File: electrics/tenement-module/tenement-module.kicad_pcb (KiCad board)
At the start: 2 copper layers, 86 x 31 mm, 27 parts, among them J2 South, J3 West, J4 East, U1 BA033CC0FP-E2, U2 MCP23009-E_SS, U3 WIRL-WMB8, U4 MAX3486

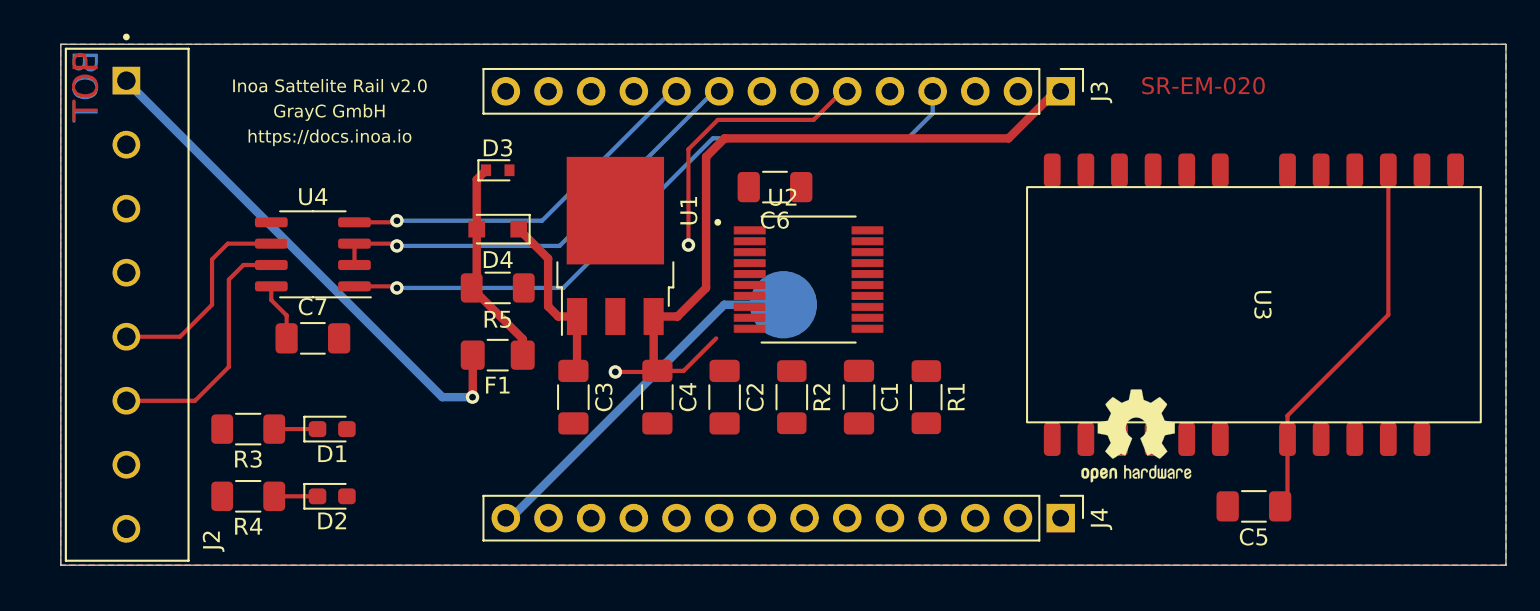
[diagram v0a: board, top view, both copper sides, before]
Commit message: Added product numbers for cost calculation
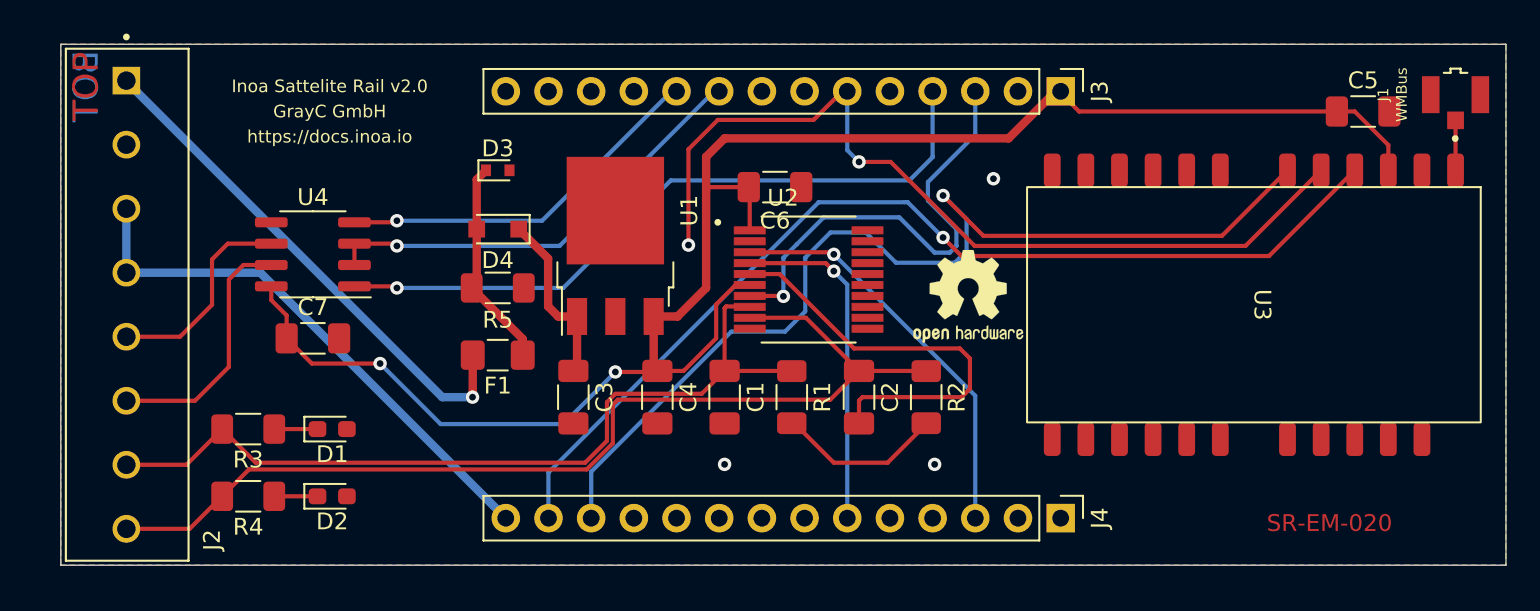
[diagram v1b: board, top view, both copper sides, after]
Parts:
- removed TP1: Shield, TestPoint:TestPoint_Pad_D4.0mm
- added J1: WMBus, footprints:IPEX_20279-001E-01, F.Cu at (183.0, 83.0)
- moved C5 24.4 mm to (177.5, 84.0), turned to 0 degrees
- moved G1 13.0 mm to (154.0, 95.0)
- moved C1 8.00 mm to (139.5, 101.0)
- moved C2 8.00 mm to (147.5, 101.0)
- moved R1 8.00 mm to (143.5, 101.0)
- moved R2 8.00 mm to (151.5, 101.0)
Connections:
- J2 pad 7: RS485_1_A -> S0_0
- J2 pad 8: RS485_1_B -> S0_1
- J3 pad 6: RS485_1_RX -> WMBus_URXD
- J4 pad 12: RS485_1_TXE -> WMBus_~{RTS}
- J4 pad 13: RS485_1_TX -> WMBus_UTXD
- U3 pad 19: +3V3 -> WMBus_~{Reset}
- U3 pad 6: WMBus_RTS -> WMBus_~{RTS}
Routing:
- net WMBus_~{RTS}: track 0.00 -> 60.9 mm, vias 0 -> 1
- net WMBus_UTXD: track 0.00 -> 60.8 mm, vias 0 -> 1
- net S0_1: track 0.02 -> 60.7 mm
- net WMBus_URXD: track 0.00 -> 52.6 mm, vias 0 -> 2
- net S0_0: track 0.02 -> 50.2 mm
- net +3V3: track 70.9 -> 113.6 mm, vias 1 -> 2
- net S0_INT: track 0.00 -> 27.7 mm, vias 0 -> 1
- net GND: track 0.00 -> 25.2 mm, vias 0 -> 3
- net I2C_SCL: track 0.00 -> 24.2 mm, vias 0 -> 1
- net I2C_SDA: track 0.00 -> 20.2 mm, vias 0 -> 1
- net RS485_1_RX: track 16.7 -> 0.00 mm, vias 1 -> 0
- net GNDPWR: track 21.9 -> 32.4 mm
- net WMBus_ANT: track 0.00 -> 2.97 mm
- net RS485_0_RX: track 40.4 -> 41.9 mm

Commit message: INOA-372 Fix out of stock components in TM module
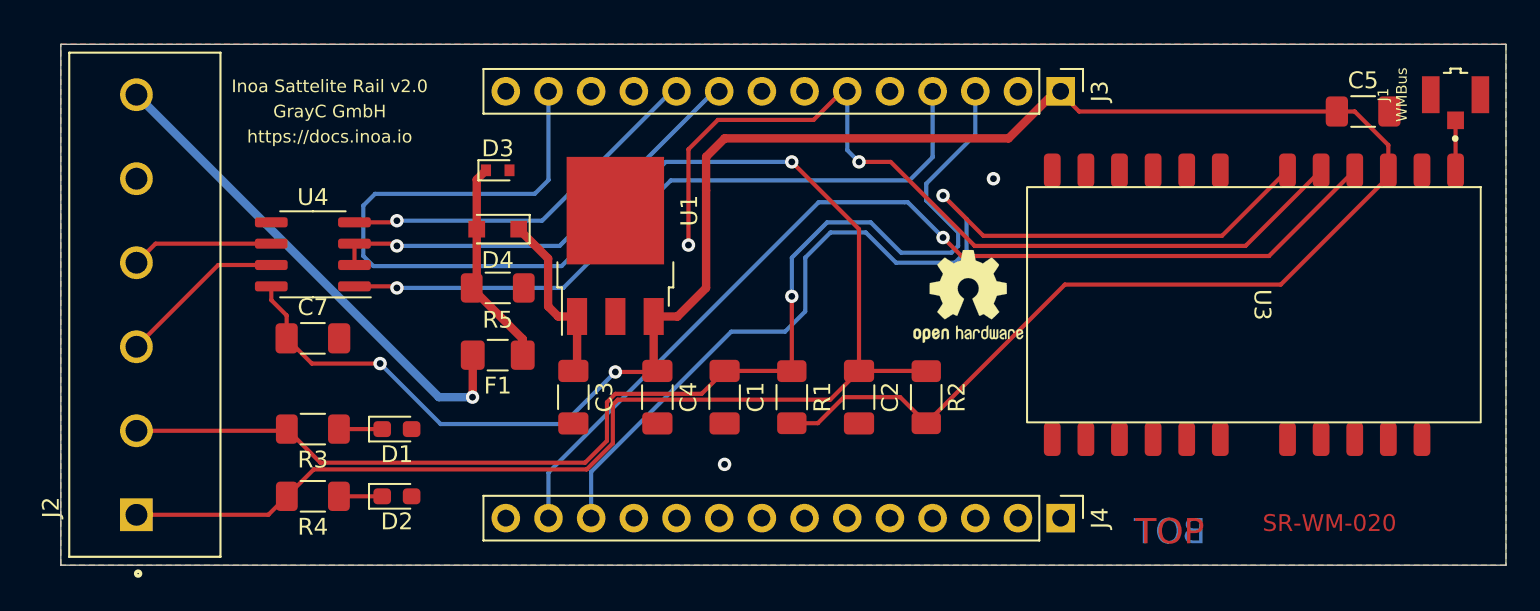
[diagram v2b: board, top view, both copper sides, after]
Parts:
- removed C6: 100nF, Capacitor_SMD:C_1206_3216Metric_Pad1.33x1.80mm_HandSolder
- removed U2: MCP23009-E_SS, footprints:SOP65P780X200-20N
- J2: value South -> North; footprint footprints:PHOENIX_1727078 -> footprints:PHOENIX_1935200
- moved D1 3.85 mm to (120.0, 102.9)
- moved D2 3.85 mm to (120.0, 106.9)
- moved R3 3.85 mm to (115.0, 102.9)
- moved R4 3.85 mm to (115.0, 106.9)
- moved J2 0.60 mm to (104.5, 95.5), turned to 90 degrees
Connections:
- J2 pad 1: VCC -> S0_1
- J2 pad 2: GND -> S0_0
- J2 pad 3: GNDPWR -> RS485_0_B
- J2 pad 4: GNDPWR -> RS485_0_A
- J2 pad 5: RS485_0_A -> GND
- J2 pad 6: RS485_0_B -> VCC
- J3 pad 13: unconnected-(J3-Pad13) -> S0_1
- J3 pad 3: S0_INT -> S0_0
- J4 pad 3: I2C_SCL -> unconnected-(J4-Pad3)
- J4 pad 6: I2C_SDA -> unconnected-(J4-Pad6)
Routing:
- net S0_1: track 60.7 -> 114.2 mm, vias 0 -> 1
- net GNDPWR: track 32.4 -> 0.00 mm
- net S0_INT: track 27.7 -> 0.00 mm, vias 1 -> 0
- net GND: track 25.2 -> 0.00 mm, vias 3 -> 2
- net I2C_SCL: track 24.2 -> 0.00 mm, vias 1 -> 0
- net S0_0: track 50.2 -> 73.3 mm, vias 0 -> 1
- net I2C_SDA: track 20.2 -> 0.00 mm, vias 1 -> 0
- net +3V3: track 113.6 -> 132.6 mm
- net RS485_0_B: track 15.0 -> 10.0 mm
- net RS485_0_A: track 12.5 -> 8.50 mm
- net VCC: track 30.9 -> 30.0 mm
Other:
- board text added: "SR-WM-020"
- board text removed: "SR-EM-020"
